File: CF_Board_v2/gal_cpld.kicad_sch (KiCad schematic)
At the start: 6 parts, among them U10 74LVC1G07, U7 GAL, U8 CPLD, U9 74LVC1G08, X2 40MHz

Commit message: Sheet title etc
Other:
- company: (none) -> (C) TOM STOREY
- title: (none) -> GAL AND CPLD CONTROL LOGIC
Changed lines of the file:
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@@
 (kicad_sch (version 20211123) (generator eeschema)
   (paper "A4")
+  (title_block
+    (title "GAL AND CPLD CONTROL LOGIC")
+    (date "2024-01-30")
+    (rev "1")
+    (company "(C) TOM STOREY")
+    (comment 1 "FREE FOR NON-COMMERCIAL USE")
+  )
   (junction (at 139.7 30.48) (diameter 0) (color 0 0 0 0)
   )

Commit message: Power and decoupling caps
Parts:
- added C10, C11, C12, C13, C14, C9: 100nF, COMET_footprints:C_SMD0805, symbol COMET_symbols:C
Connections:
- net +5V: now also U7.1 (*VCC), U7.28 (VCC), U8.15 (VCC), U8.23 (VCC), U8.3 (VCC), U8.35 (VCC), C10.1, C11.1, C12.1, C13.1, C14.1, C9.1
- net GND: now also U7.14 (GND), U7.15 (GND*), U7.22 (GND*), U7.8 (GND*), U8.10 (GND), U8.22 (GND), U8.30 (GND), U8.42 (GND), C10.2, C11.2, C12.2, C13.2, C14.2, C9.2
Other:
- moved on the sheet: U7B, U8C

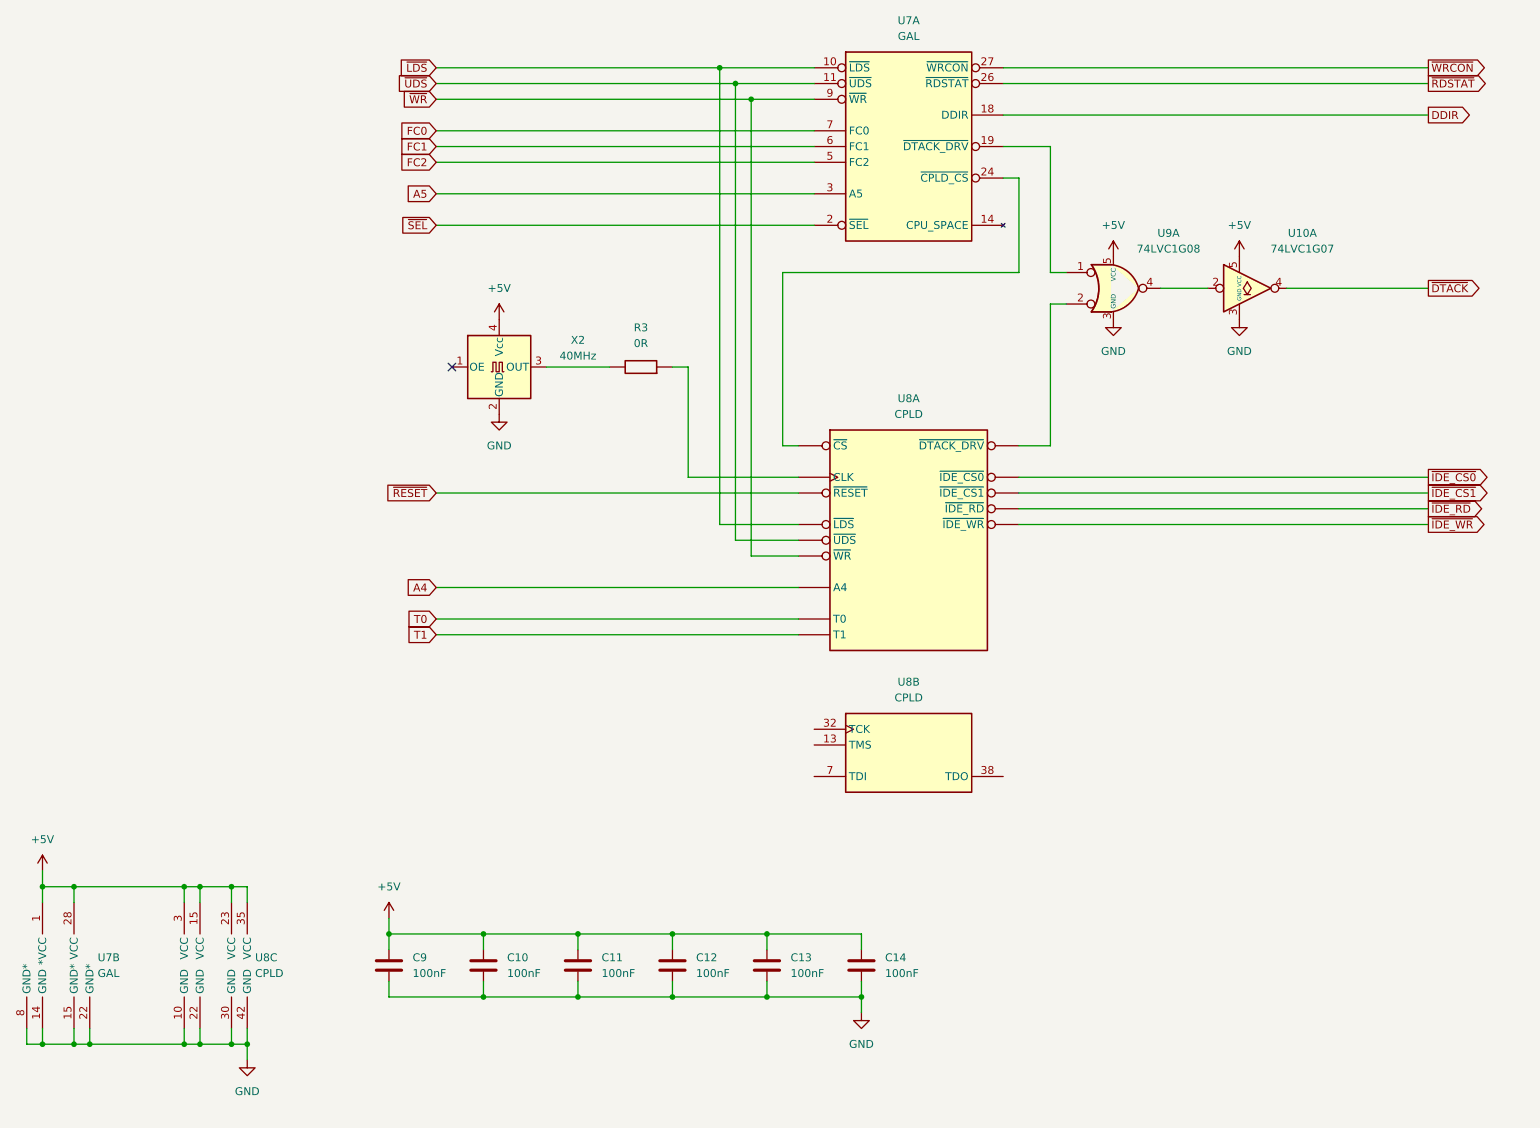
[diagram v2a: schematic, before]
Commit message: Add IDE DBEN logic and read pull up resistors
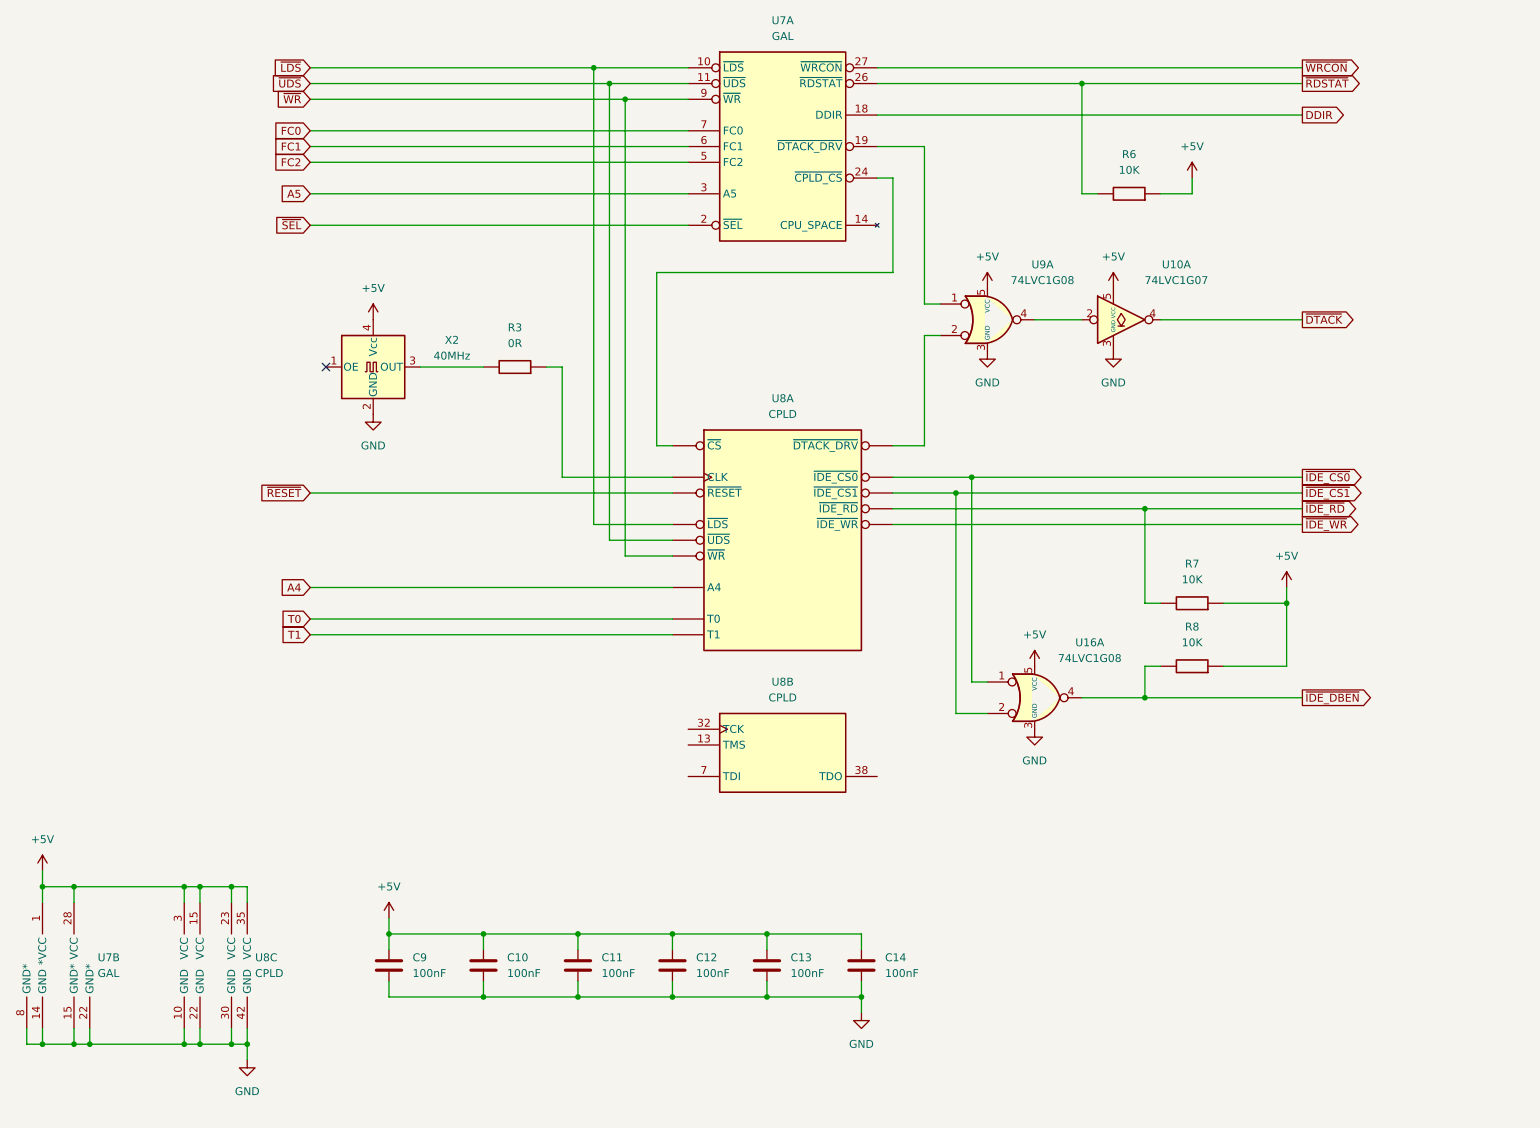
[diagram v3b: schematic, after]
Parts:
- added R6, R7, R8: 10K, COMET_footprints:R_SMD0805, symbol COMET_symbols:R
- added U16: 74LVC1G08, COMET_footprints:Package_SOT23-5, symbol COMET_symbols:74x1G08
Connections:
- net +5V: now also R6.2, R7.2, R8.2, U16.5 (VCC)
- net GND: now also U16.3 (GND)
- net ~{IDE_CS0}: now also U16.1
- net ~{IDE_CS1}: now also U16.2
- net ~{IDE_RD}: now also R7.1
- net ~{RDSTAT}: now also R6.1
- new net ~{IDE_DBEN}: R8.1, U16.4
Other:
- moved on the sheet: R3, U10A, U7A, U8A, U8B, U9A, X2

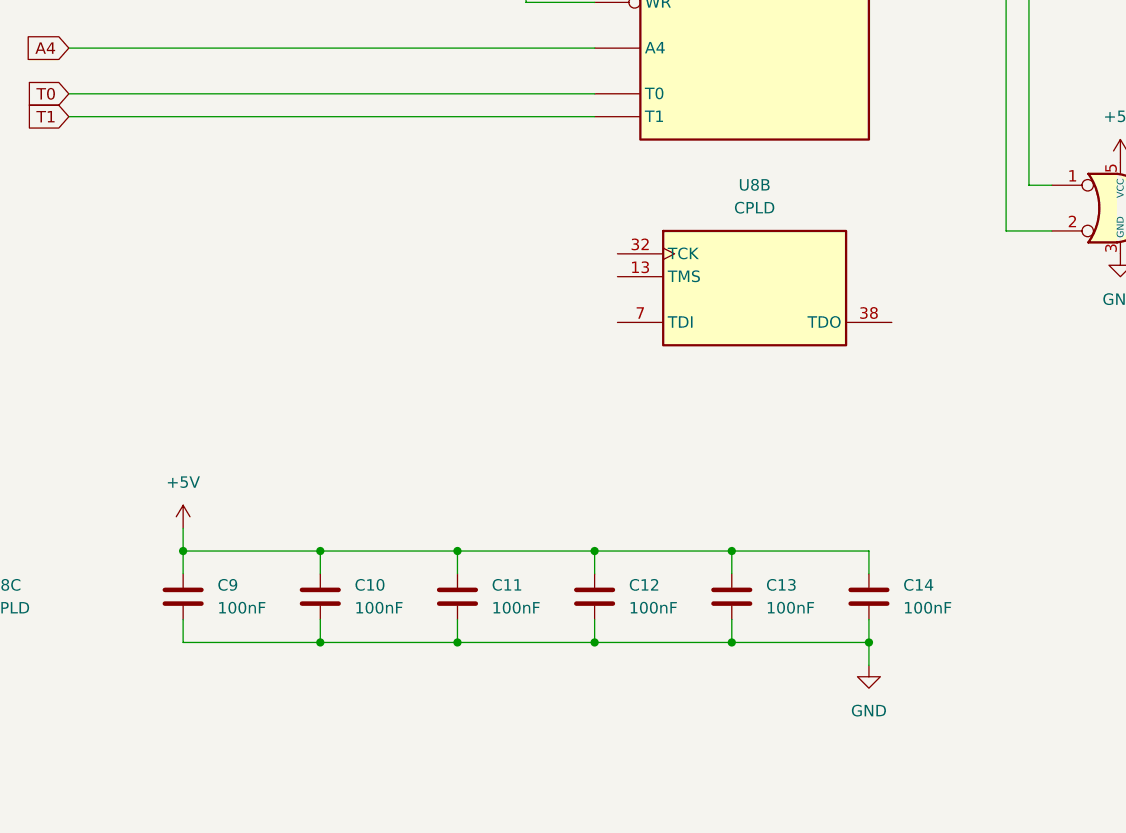
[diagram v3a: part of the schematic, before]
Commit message: Finish JTAG header circuitry
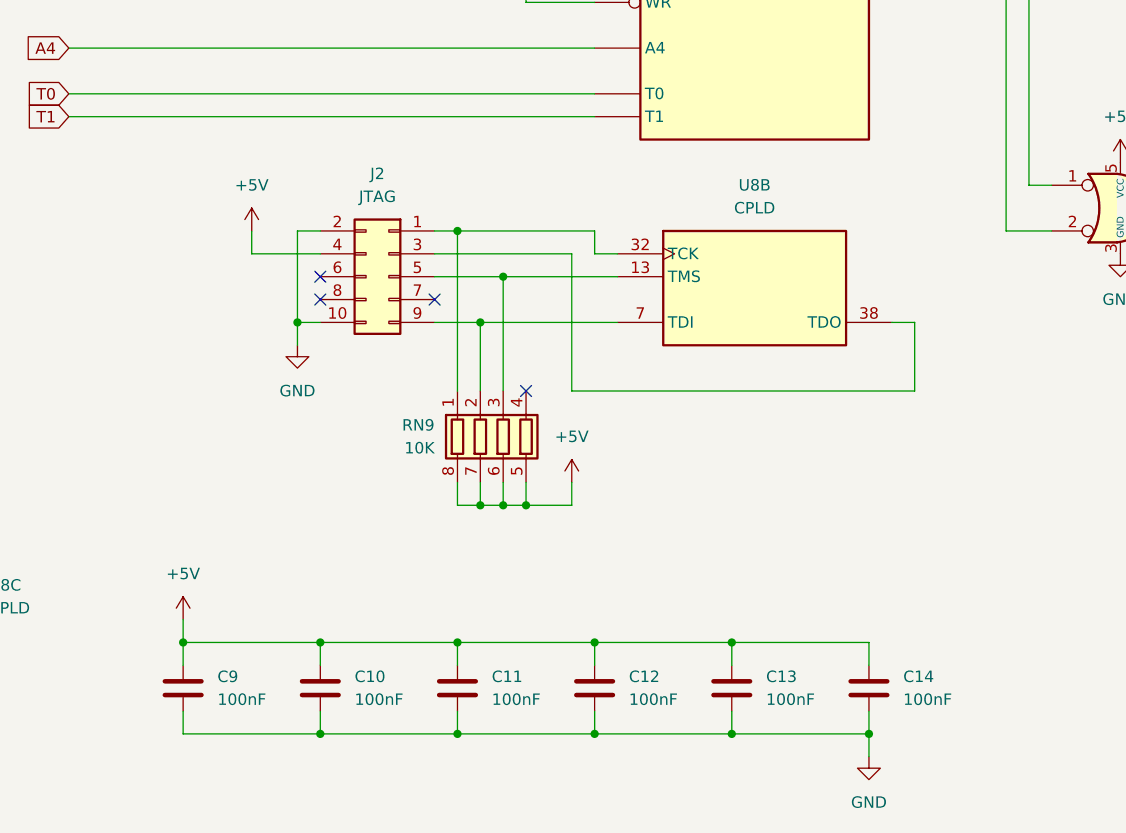
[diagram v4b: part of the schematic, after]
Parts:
- added J2: JTAG, Connector_PinHeader_2.54mm:PinHeader_2x05_P2.54mm_Vertical, symbol Connector_Generic:Conn_02x05_Odd_Even
- added RN9: 10K, symbol Device:R_Pack04
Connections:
- net +5V: now also J2.4 (Pin_4), RN9.5 (R4.2), RN9.6 (R3.2), RN9.7 (R2.2), RN9.8 (R1.2)
- net GND: now also J2.10 (Pin_10), J2.2 (Pin_2)
- net at U8.13 (TMS): now also J2.5 (Pin_5), RN9.3 (R3.1)
- net at U8.32 (TCK): now also J2.1 (Pin_1), RN9.1 (R1.1)
- net at U8.38 (TDO): now also J2.3 (Pin_3)
- net at U8.7 (TDI): now also J2.9 (Pin_9), RN9.2 (R2.1)
- no-connect marks 1 -> 5
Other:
- moved on the sheet: C10, C11, C12, C13, C14, C9

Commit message: Add footprints
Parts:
- RN9: footprint (none) -> Resistor_SMD:R_Cat16-4
- U7: footprint (none) -> COMET_footprints:Package_PLCC-28_SMD_socket
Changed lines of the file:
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@@
     (property "Reference" "U7" (id 0) (at 144.78 17.78 0))
     (property "Value" "GAL" (id 1) (at 144.78 20.32 0))
-    (property "Footprint" "" (id 2) (at 144.78 48.26 0)
+    (property "Footprint" "COMET_footprints:Package_PLCC-28_SMD_socket" (id 2) (at 144.78 48.26 0)
       (effects (font (size 1.27 1.27)) hide)
     )
@@
       (effects (font (size 1.27 1.27)) (justify left))
     )
-    (property "Footprint" "" (id 2) (at 27.94 180.34 0)
+    (property "Footprint" "COMET_footprints:Package_PLCC-28_SMD_socket" (id 2) (at 27.94 180.34 0)
       (effects (font (size 1.27 1.27)) hide)
     )
@@
       (effects (font (size 1.27 1.27)) (justify right))
     )
-    (property "Footprint" "" (id 2) (at 123.825 152.4 90)
-      (effects (font (size 1.27 1.27)) hide)
-    )
+    (property "Footprint" "Resistor_SMD:R_Cat16-4" (id 2) (at 123.825 152.4 90)
+      (effects (font (size 1.27 1.27)) hide)
+    )
